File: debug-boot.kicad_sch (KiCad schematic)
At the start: 11 parts, among them J1 61300311121, J2 61300511121, J3 Conn_ARM_JTAG_SWD_10, J4 61300311121, J5 61300311121

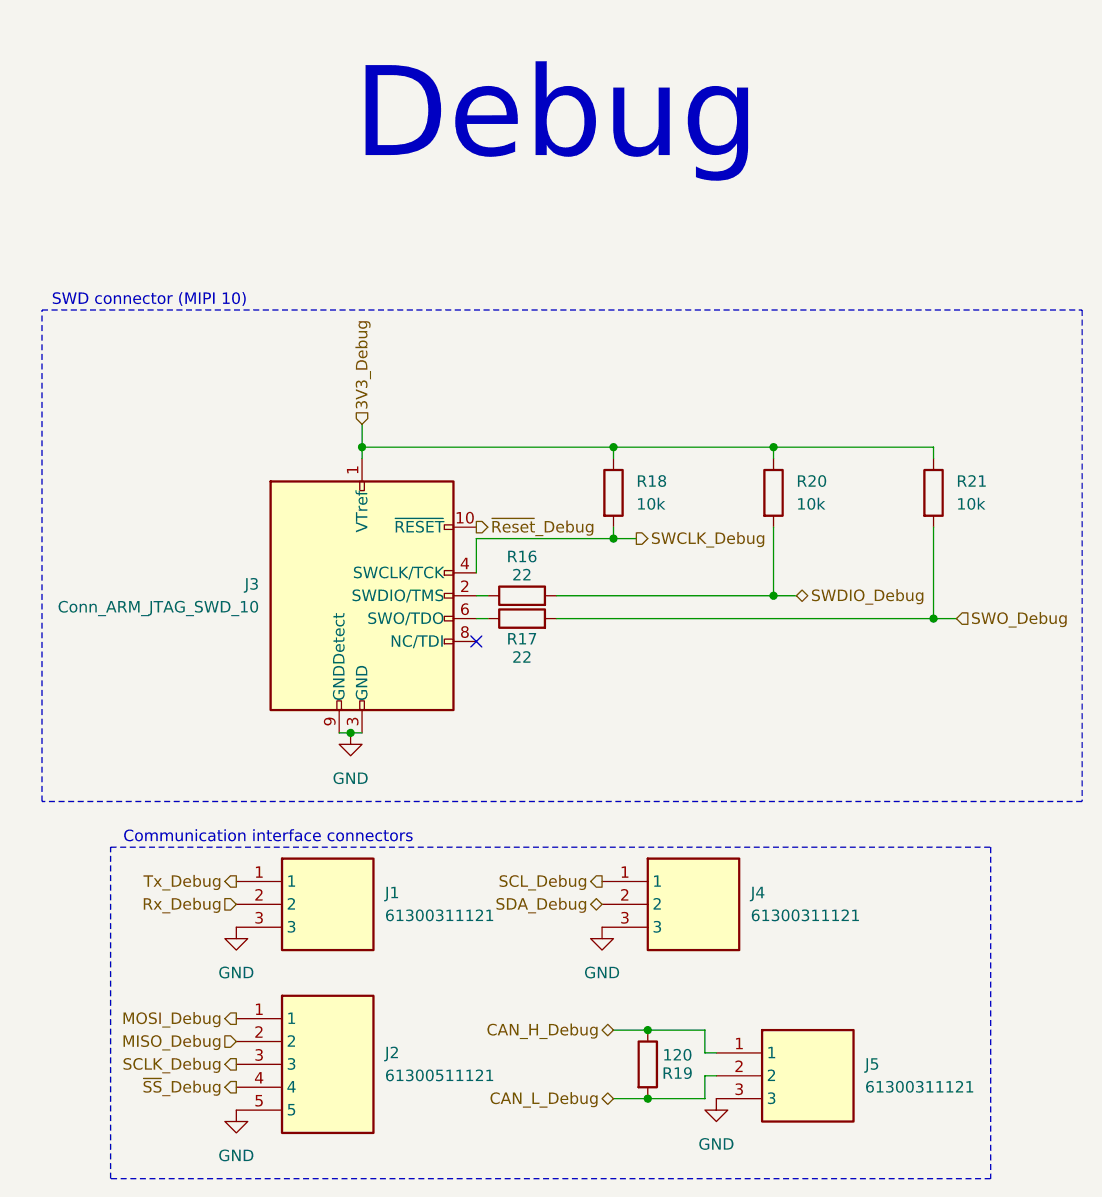
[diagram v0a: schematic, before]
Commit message: Move SWD debug connector from debug sheet to MCU sheet
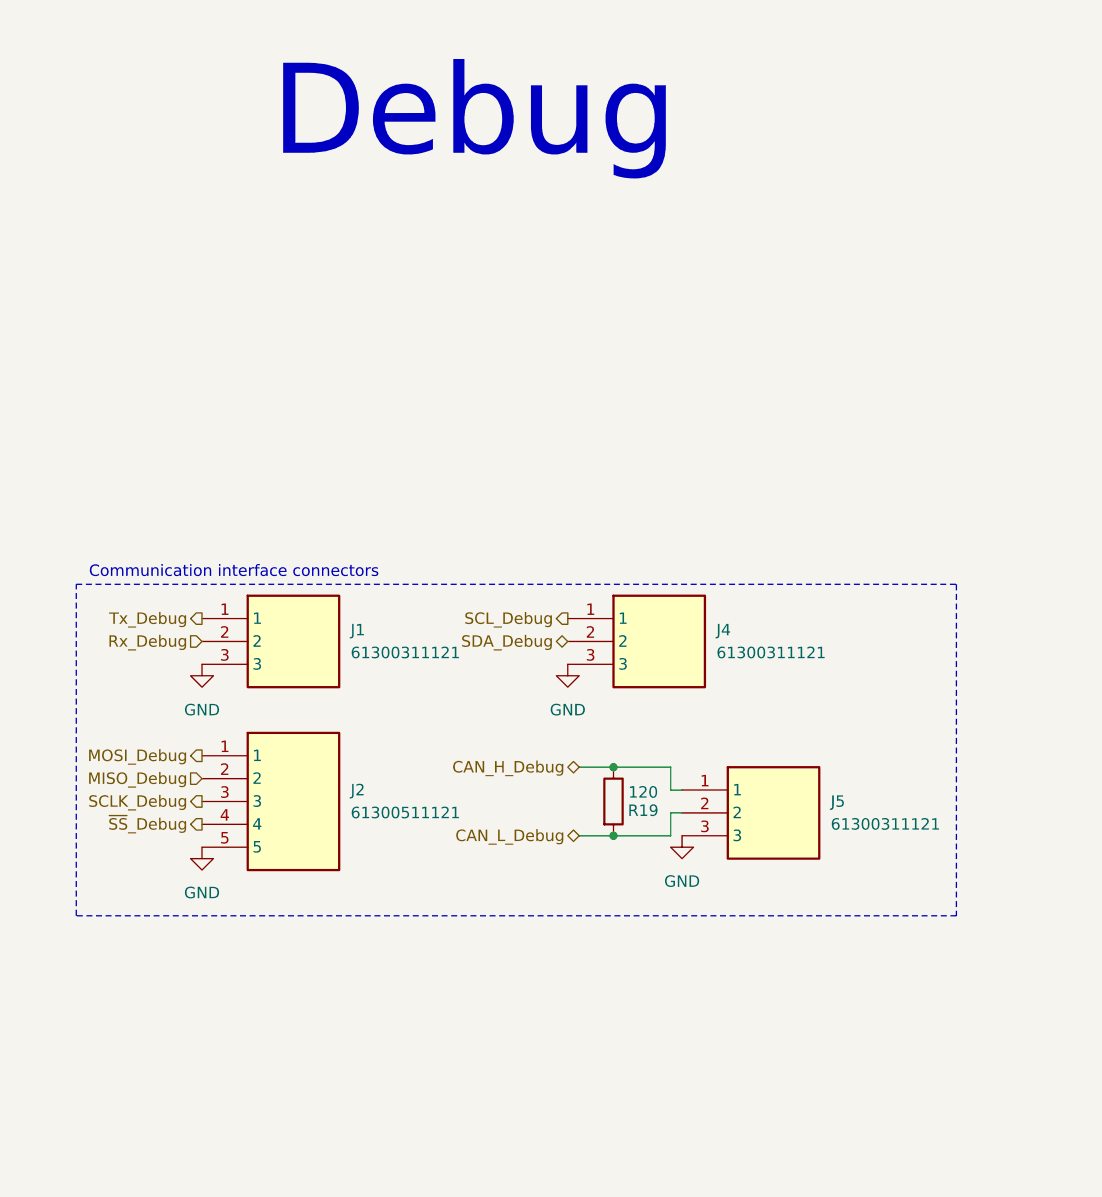
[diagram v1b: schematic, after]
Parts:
- removed J3: Conn_ARM_JTAG_SWD_10, weather-station-poc-fp:FTSH10501LDVK, symbol Connector:Conn_ARM_JTAG_SWD_10
- removed R16, R17: 22, Resistor_SMD:R_0603_1608Metric_Pad0.98x0.95mm_HandSolder, symbol Device:R
- removed R18, R20, R21: 10k, Resistor_SMD:R_0603_1608Metric_Pad0.98x0.95mm_HandSolder, symbol Device:R
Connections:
- no-connect marks 1 -> 0
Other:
- note removed: "SWD connector (MIPI 10)"
- moved on the sheet: J1, J2, J4, J5, R19
